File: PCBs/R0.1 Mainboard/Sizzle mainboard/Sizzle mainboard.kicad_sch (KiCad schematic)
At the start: 36 parts, among them J1 X Stepper, J2 Screen, J3 USB_C_Receptacle_USB2.0_16P, J4 Debug, J5 Z Stepper, J6 Y Stepper, J7 UV light, Q1 Q_NMOS_GSD, SW1 SW_Push, U1 STM32F401RCTx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

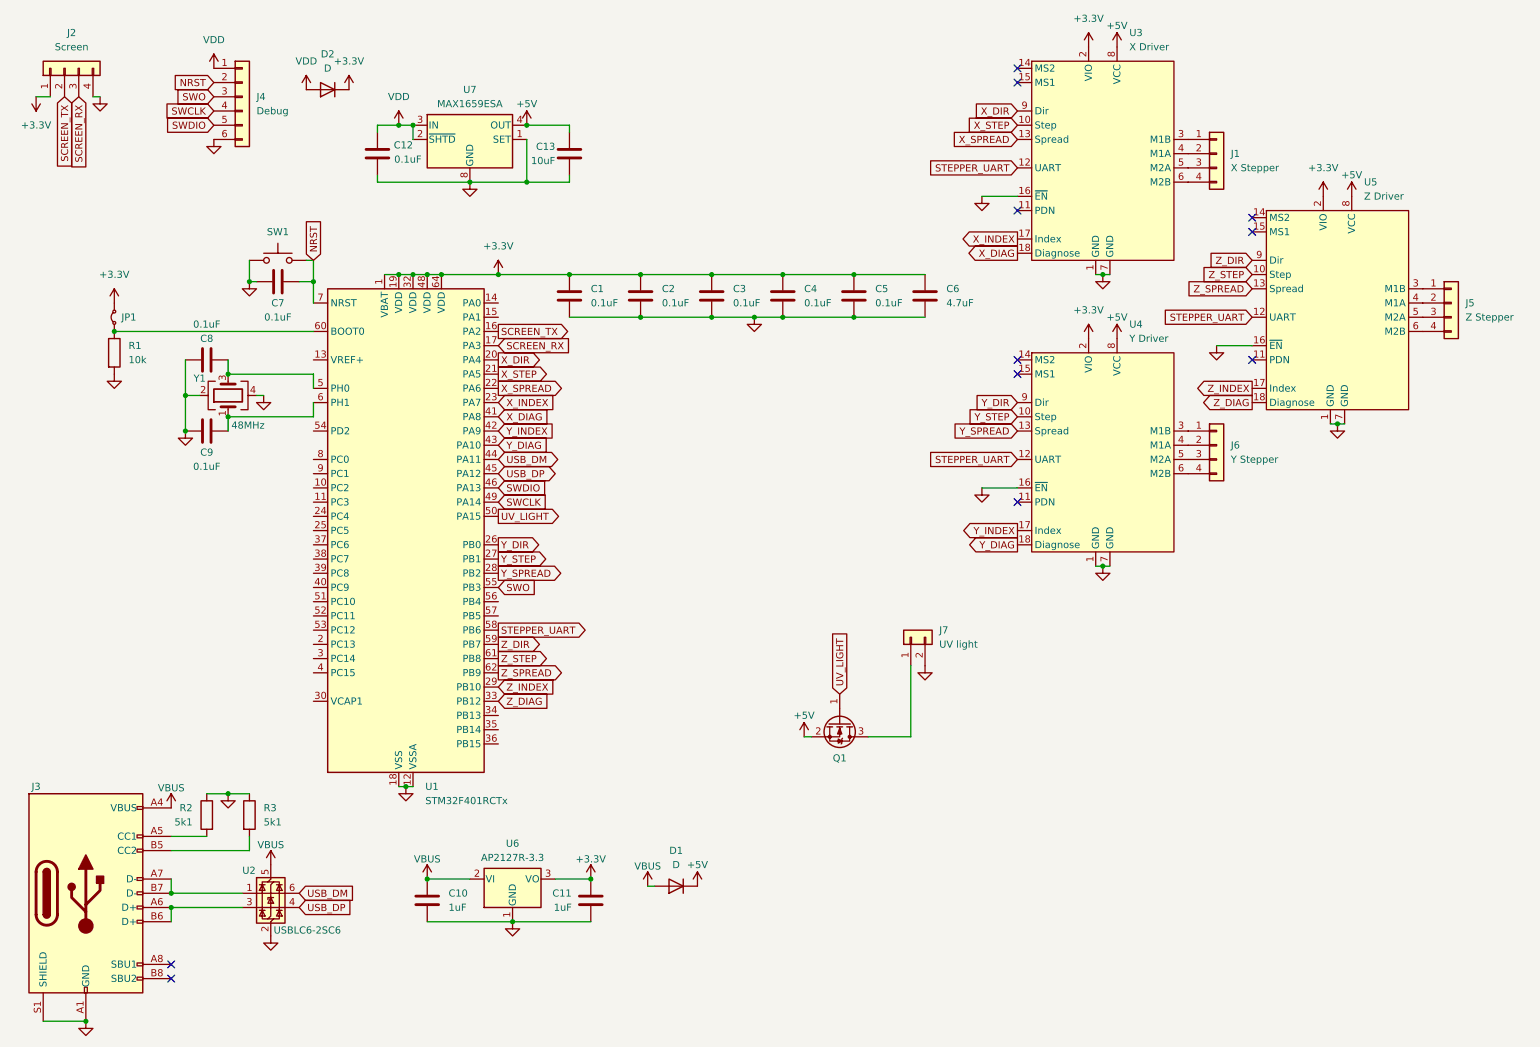
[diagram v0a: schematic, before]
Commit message: Reorganize, add missing capacitors to MCU
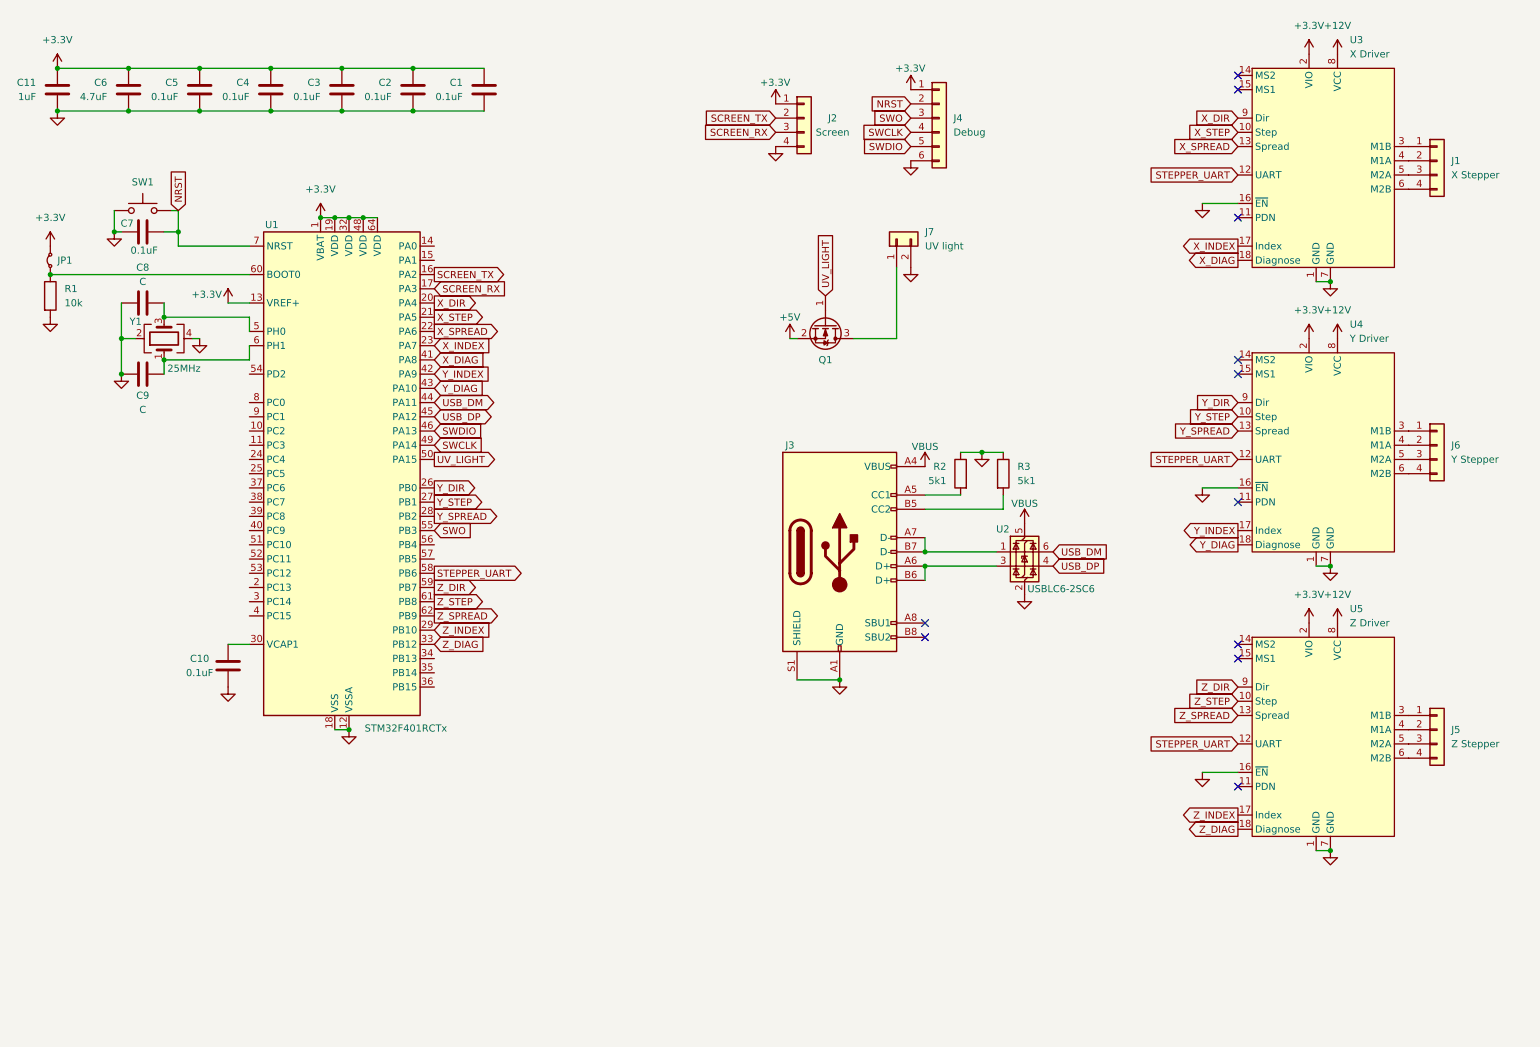
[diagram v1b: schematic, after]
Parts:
- removed C12: 0.1uF, symbol Device:C
- removed C13: 10uF, symbol Device:C
- removed D1, D2: D, symbol Device:D
- removed U6: AP2127R-3.3, Package_TO_SOT_SMD:SOT-89-3, symbol Regulator_Linear:AP2127R-3.3
- removed U7: MAX1659ESA, Package_SO:SOIC-8_3.9x4.9mm_P1.27mm, symbol Regulator_Linear:MAX1659ESA
- C10: value 1uF -> 0.1uF
- C8, C9: value 0.1uF -> C
- Y1: value 48MHz -> 25MHz
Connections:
- net VDD is gone; now on net +3.3V: J4.1 (Pin_1)
- net +3.3V: now also U1.13 (VREF+)
- net +5V: no longer U3.8 (VCC), U4.8 (VCC), U5.8 (VCC)
- net VBUS: no longer C10.1
- net at U1.30 (VCAP1): now also C10.1
- new net +12V: U3.8 (VCC), U4.8 (VCC), U5.8 (VCC)
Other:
- moved on the sheet: C1, C2, C3, C4, C5, C6, C7, C8, C9, J1, J2, J3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
